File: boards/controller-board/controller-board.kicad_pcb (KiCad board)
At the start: 2 copper layers, 130 x 115 mm, 226 parts, among them IC10 A6214KLKTR-T, IC11 A6214KLKTR-T, IC12 A6214KLKTR-T, IC13 A6214KLKTR-T, IC2 A6214KLKTR-T, IC3 A6214KLKTR-T, IC4 A6214KLKTR-T, IC5 A6214KLKTR-T, IC6 A6214KLKTR-T, IC7 A6214KLKTR-T, IC8 A6214KLKTR-T, IC9 A6214KLKTR-T, J1 Conn_01x02, J2 Conn_01x02, J3 Conn_01x02, J4 Conn_01x02, J5 Conn_01x03, J6 Phoenix 1995499, Q1 PMV45EN, Q2 Goford_G11S_20V_11A, SW1 EG1271, U1 LTC3624, U2 ADS1015IRUGR, U3 ADS1015IRUGR, U4 RPi_Pico, U5 MCP4728

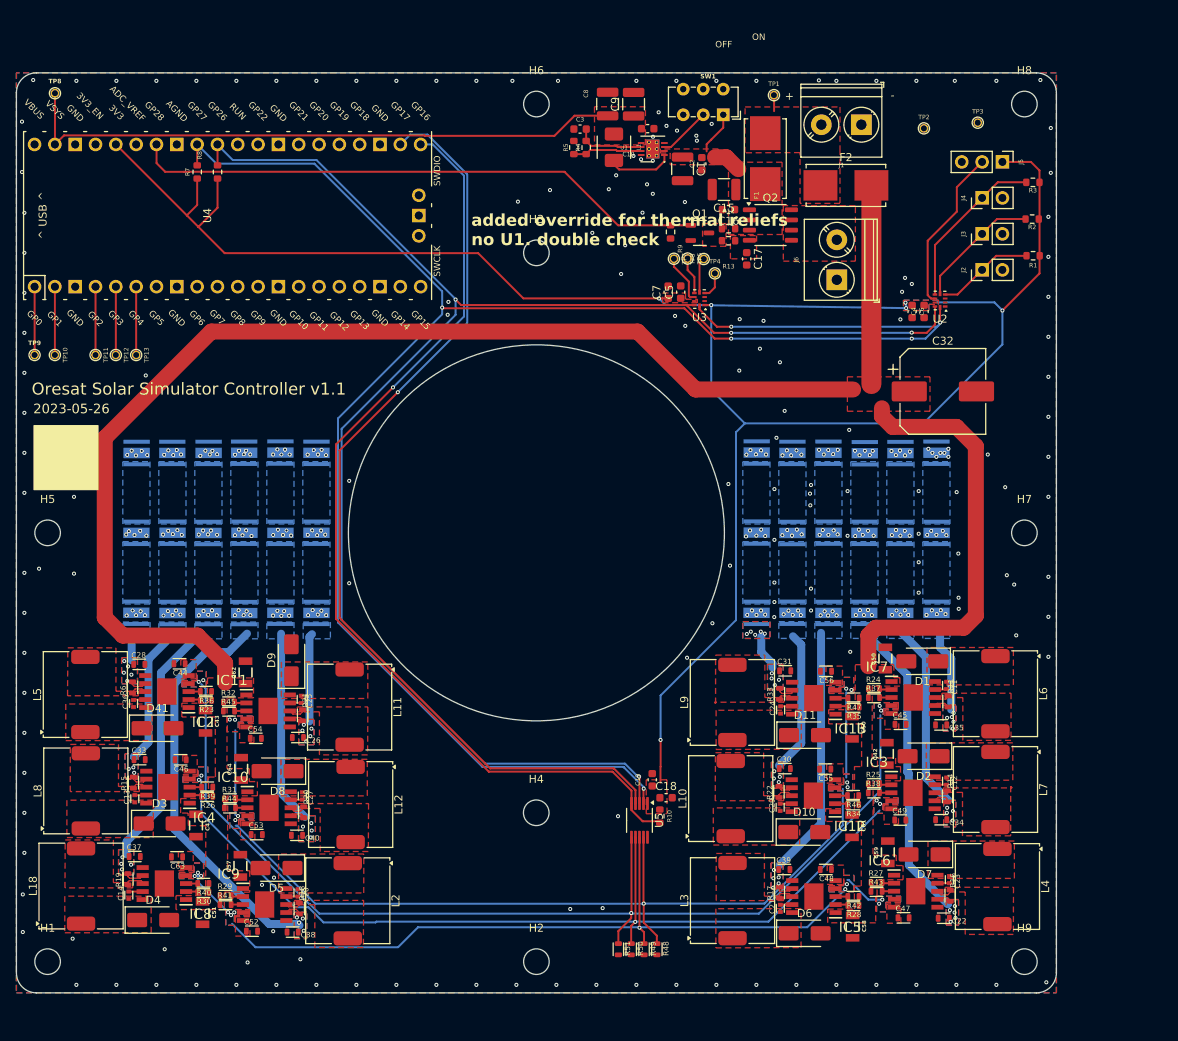
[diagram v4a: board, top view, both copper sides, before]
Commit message: polished reference designators
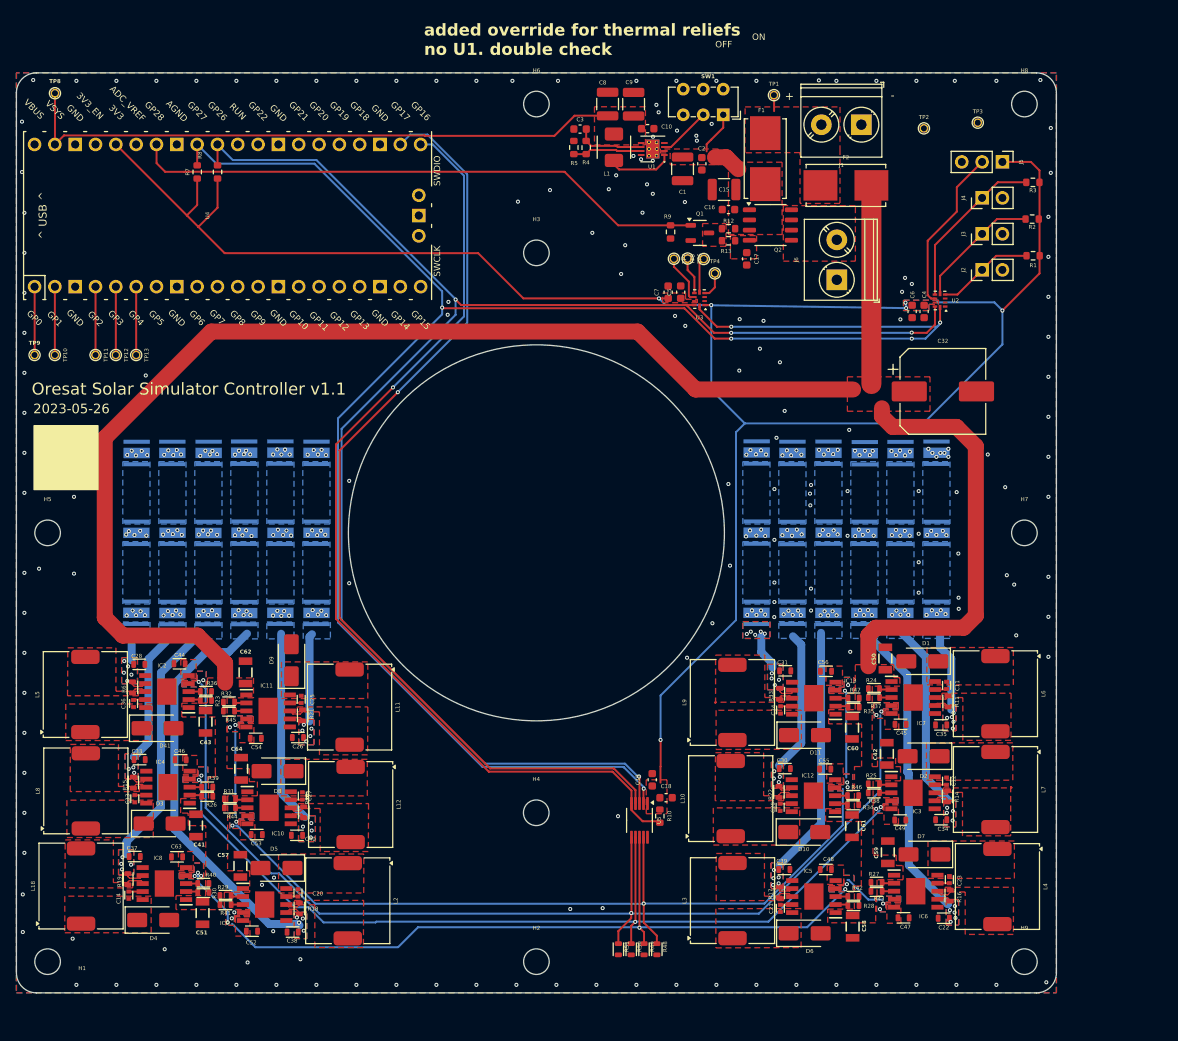
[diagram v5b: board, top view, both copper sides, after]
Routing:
- net BLUE_LIM: track 106.9 -> 107.6 mm
- net RED_LIM: track 135.0 -> 135.6 mm
